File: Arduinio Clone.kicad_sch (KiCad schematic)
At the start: 12 parts, among them U1 DS1337_GM, U2 24LC1025, U3 ATmega328P-A, Y1 Crystal, Y2 Crystal

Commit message: Component associations and values
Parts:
- BT1: value Battery -> (none)
- C1, C2: value C -> (none)
- C3: value C_Polarized -> (none)
- D1: value LED -> (none)
- R1, R2: value R -> (none)
- U1: value DS1337_GM -> (none)
- U2: value 24LC1025 -> (none)
- U3: value ATmega328P-A -> (none); footprint Package_QFP:TQFP-32_7x7mm_P0.8mm -> (none)
- Y1, Y2: value Crystal -> (none)
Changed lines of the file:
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@@
     (in_bom yes) (on_board yes) (fields_autoplaced)
     (property "Reference" "D1" (id 0) (at 127.9525 68.58 0))
-    (property "Value" "LED" (id 1) (at 127.9525 71.12 0))
+    (property "Value" "" (id 1) (at 127.9525 71.12 0))
     (property "Footprint" "" (id 2) (at 129.54 74.93 0)
       (effects (font (size 1.27 1.27)) hide)
@@
       (effects (font (size 1.27 1.27)) (justify left))
     )
-    (property "Value" "24LC1025" (id 1) (at 51.5494 91.44 0)
+    (property "Value" "" (id 1) (at 51.5494 91.44 0)
       (effects (font (size 1.27 1.27)) (justify left))
     )
@@
     (in_bom yes) (on_board yes) (fields_autoplaced)
     (property "Reference" "Y1" (id 0) (at 29.21 60.96 0))
-    (property "Value" "Crystal" (id 1) (at 29.21 63.5 0))
+    (property "Value" "" (id 1) (at 29.21 63.5 0))
     (property "Footprint" "" (id 2) (at 29.21 68.58 0)
       (effects (font (size 1.27 1.27)) hide)
@@
       (effects (font (size 1.27 1.27)) (justify left))
     )
-    (property "Value" "C_Polarized" (id 1) (at 223.52 79.1209 0)
+    (property "Value" "" (id 1) (at 223.52 79.1209 0)
       (effects (font (size 1.27 1.27)) (justify left))
     )
@@
       (effects (font (size 1.27 1.27)) (justify left))
     )
-    (property "Value" "DS1337_GM" (id 1) (at 51.5494 63.5 0)
+    (property "Value" "" (id 1) (at 51.5494 63.5 0)
       (effects (font (size 1.27 1.27)) (justify left))
     )
@@
     (pin "8")
   )
+  (symbol (lib_id "power:GND") (at 218.44 114.3 0) (unit 1)
+    (in_bom yes) (on_board yes) (fields_autoplaced)
+    (property "Reference" "#PWR0101" (id 0) (at 218.44 120.65 0)
+      (effects (font (size 1.27 1.27)) hide)
+    )
+    (property "Value" "" (id 1) (at 218.44 119.38 0))
+    (property "Footprint" "" (id 2) (at 218.44 114.3 0)
+      (effects (font (size 1.27 1.27)) hide)
+    )
+    (property "Datasheet" "" (id 3) (at 218.44 114.3 0)
+      (effects (font (size 1.27 1.27)) hide)
+    )
+    (pin "1")
+  )
   (symbol (lib_id "MCU_Microchip_ATmega:ATmega328P-A") (at 163.83 86.36 0) (unit 1)
     (in_bom yes) (on_board yes) (fields_autoplaced)
@@
       (effects (font (size 1.27 1.27)) (justify left))
     )
-    (property "Value" "ATmega328P-A" (id 1) (at 165.8494 127 0)
-      (effects (font (size 1.27 1.27)) (justify left))
-    )
-    (property "Footprint" "Package_QFP:TQFP-32_7x7mm_P0.8mm" (id 2) (at 163.83 86.36 0)
+    (property "Value" "" (id 1) (at 165.8494 127 0)
+      (effects (font (size 1.27 1.27)) (justify left))
+    )
+    (property "Footprint" "" (id 2) (at 163.83 86.36 0)
       (effects (font (size 1.27 1.27) italic) hide)
     )
@@
       (effects (font (size 1.27 1.27)) (justify left))
     )
-    (property "Value" "C" (id 1) (at 95.25 57.1499 0)
+    (property "Value" "" (id 1) (at 95.25 57.1499 0)
       (effects (font (size 1.27 1.27)) (justify left))
     )
@@
       (effects (font (size 1.27 1.27)) (justify left))
     )
-    (property "Value" "R" (id 1) (at 115.57 86.3599 0)
+    (property "Value" "" (id 1) (at 115.57 86.3599 0)
       (effects (font (size 1.27 1.27)) (justify left))
     )
@@
       (effects (font (size 1.27 1.27)) (justify left))
     )
-    (property "Value" "Battery" (id 1) (at 223.52 59.3089 0)
+    (property "Value" "" (id 1) (at 223.52 59.3089 0)
       (effects (font (size 1.27 1.27)) (justify left))
     )
@@
     (in_bom yes) (on_board yes) (fields_autoplaced)
     (property "Reference" "Y2" (id 0) (at 102.87 60.96 0))
-    (property "Value" "Crystal" (id 1) (at 102.87 63.5 0))
+    (property "Value" "" (id 1) (at 102.87 63.5 0))
     (property "Footprint" "" (id 2) (at 102.87 68.58 0)
       (effects (font (size 1.27 1.27)) hide)
@@
       (effects (font (size 1.27 1.27)) (justify left))
     )
-    (property "Value" "R" (id 1) (at 135.89 93.9799 0)
+    (property "Value" "" (id 1) (at 135.89 93.9799 0)
       (effects (font (size 1.27 1.27)) (justify left))
     )
@@
       (effects (font (size 1.27 1.27)) (justify left))
     )
-    (property "Value" "C" (id 1) (at 95.25 67.3099 0)
+    (property "Value" "" (id 1) (at 95.25 67.3099 0)
       (effects (font (size 1.27 1.27)) (justify left))
     )
@@
   )
   (symbol_instances
+    (path "/7ea0c4cd-c3ff-478c-a95a-bb805f72808a"
+      (reference "#PWR0101") (unit 1) (value "GND") (footprint "")
+    )
     (path "/cb99d522-d98f-4f2e-af24-39a642a2262c"
-      (reference "BT1") (unit 1) (value "Battery") (footprint "")
+      (reference "BT1") (unit 1) (value "Battery 3V") (footprint "Connector_PinHeader_2.54mm:PinHeader_1x02_P2.54mm_Vertical")
     )
     (path "/a0a7411e-2ace-431e-9190-e1efd84cfa19"
-      (reference "C1") (unit 1) (value "C") (footprint "")
+      (reference "C1") (unit 1) (value "220pF") (footprint "Capacitor_SMD:C_0805_2012Metric")
     )
     (path "/f4cd744f-86c3-401e-9dc4-f3966535b983"
-      (reference "C2") (unit 1) (value "C") (footprint "")
+      (reference "C2") (unit 1) (value "220pF") (footprint "Capacitor_SMD:C_0805_2012Metric")
     )
     (path "/47ac9772-3d12-4e4c-be34-49c86c4d11b8"
-      (reference "C3") (unit 1) (value "C_Polarized") (footprint "")
+      (reference "C3") (unit 1) (value "10uF") (footprint "Capacitor_SMD:C_0805_2012Metric")
     )
     (path "/10f0ad0a-5347-4cd8-9e8b-b551768717e1"
-      (reference "D1") (unit 1) (value "LED") (footprint "")
+      (reference "D1") (unit 1) (value "LED") (footprint "LED_SMD:LED_0805_2012Metric")
     )
     (path "/99dcd93f-6742-4b81-a071-043df0a32b88/dd61ea61-ee00-483a-9cf3-44579a861992"
-      (reference "J1") (unit 1) (value "Conn_01x04") (footprint "")
+      (reference "J1") (unit 1) (value "Serial") (footprint "Connector_PinHeader_2.54mm:PinHeader_1x04_P2.54mm_Vertical")
     )
     (path "/99dcd93f-6742-4b81-a071-043df0a32b88/627a6bb9-dcd8-4955-91b8-8ac1c7ba0267"
-      (reference "J2") (unit 1) (value "Conn_01x09") (footprint "")
+      (reference "J2") (unit 1) (value "Digital Pins") (footprint "Connector_PinHeader_2.54mm:PinHeader_1x09_P2.54mm_Vertical")
     )
     (path "/99dcd93f-6742-4b81-a071-043df0a32b88/70a1e371-96bd-43fc-8ac7-1645345d3e46"
-      (reference "J3") (unit 1) (value "Conn_02x03_Odd_Even") (footprint "")
+      (reference "J3") (unit 1) (value "ICSP") (footprint "Connector_PinHeader_2.54mm:PinHeader_2x03_P2.54mm_Vertical")
     )
     (path "/99dcd93f-6742-4b81-a071-043df0a32b88/b8095f78-b7cb-4edb-8f3b-82dfbdf61388"
-      (reference "J4") (unit 1) (value "Conn_01x04") (footprint "")
+      (reference "J4") (unit 1) (value "I2C") (footprint "Connector_PinHeader_2.54mm:PinHeader_1x04_P2.54mm_Vertical")
     )
     (path "/a514a1f9-319e-4854-bd4a-fb2006c92301"
-      (reference "R1") (unit 1) (value "R") (footprint "")
+      (reference "R1") (unit 1) (value "330") (footprint "Resistor_SMD:R_0805_2012Metric_Pad1.20x1.40mm_HandSolder")
     )
     (path "/e1e0cd89-7085-4b67-b9fa-c00a933b2bea"
-      (reference "R2") (unit 1) (value "R") (footprint "")
+      (reference "R2") (unit 1) (value "10k") (footprint "Resistor_SMD:R_0805_2012Metric_Pad1.20x1.40mm_HandSolder")
     )
     (path "/5184beda-4204-4a1a-836c-6ca14ccda6ee"
-      (reference "U1") (unit 1) (value "DS1337_GM") (footprint "")
+      (reference "U1") (unit 1) (value "DS1337_GM") (footprint "Package_SO:SO-8_5.3x6.2mm_P1.27mm")
     )
     (path "/243ad795-d45f-41d7-b66a-04b2d1180b1c"
-      (reference "U2") (unit 1) (value "24LC1025") (footprint "")
+      (reference "U2") (unit 1) (value "24LC1025") (footprint "Package_SO:SOIC-8_3.9x4.9mm_P1.27mm")
     )
     (path "/7f29ecb0-6265-4d60-8278-7704387a2057"
@@
     )
     (path "/3fb113a1-a012-4b2e-a31d-61ea5b0c93b6"
-      (reference "Y1") (unit 1) (value "Crystal") (footprint "")
+      (reference "Y1") (unit 1) (value "Crystal 32MHz") (footprint "Crystal:Crystal_SMD_MicroCrystal_CC7V-T1A-2Pin_3.2x1.5mm")
     )
     (path "/d8dd4a5f-dc16-4ac5-8b31-704bbe349563"
-      (reference "Y2") (unit 1) (value "Crystal") (footprint "")
-    )
-  )
+      (reference "Y2") (unit 1) (value "Crystal 16MHz") (footprint "Crystal:Crystal_SMD_5032-2Pin_5.0x3.2mm_HandSoldering")
+    )
+  )

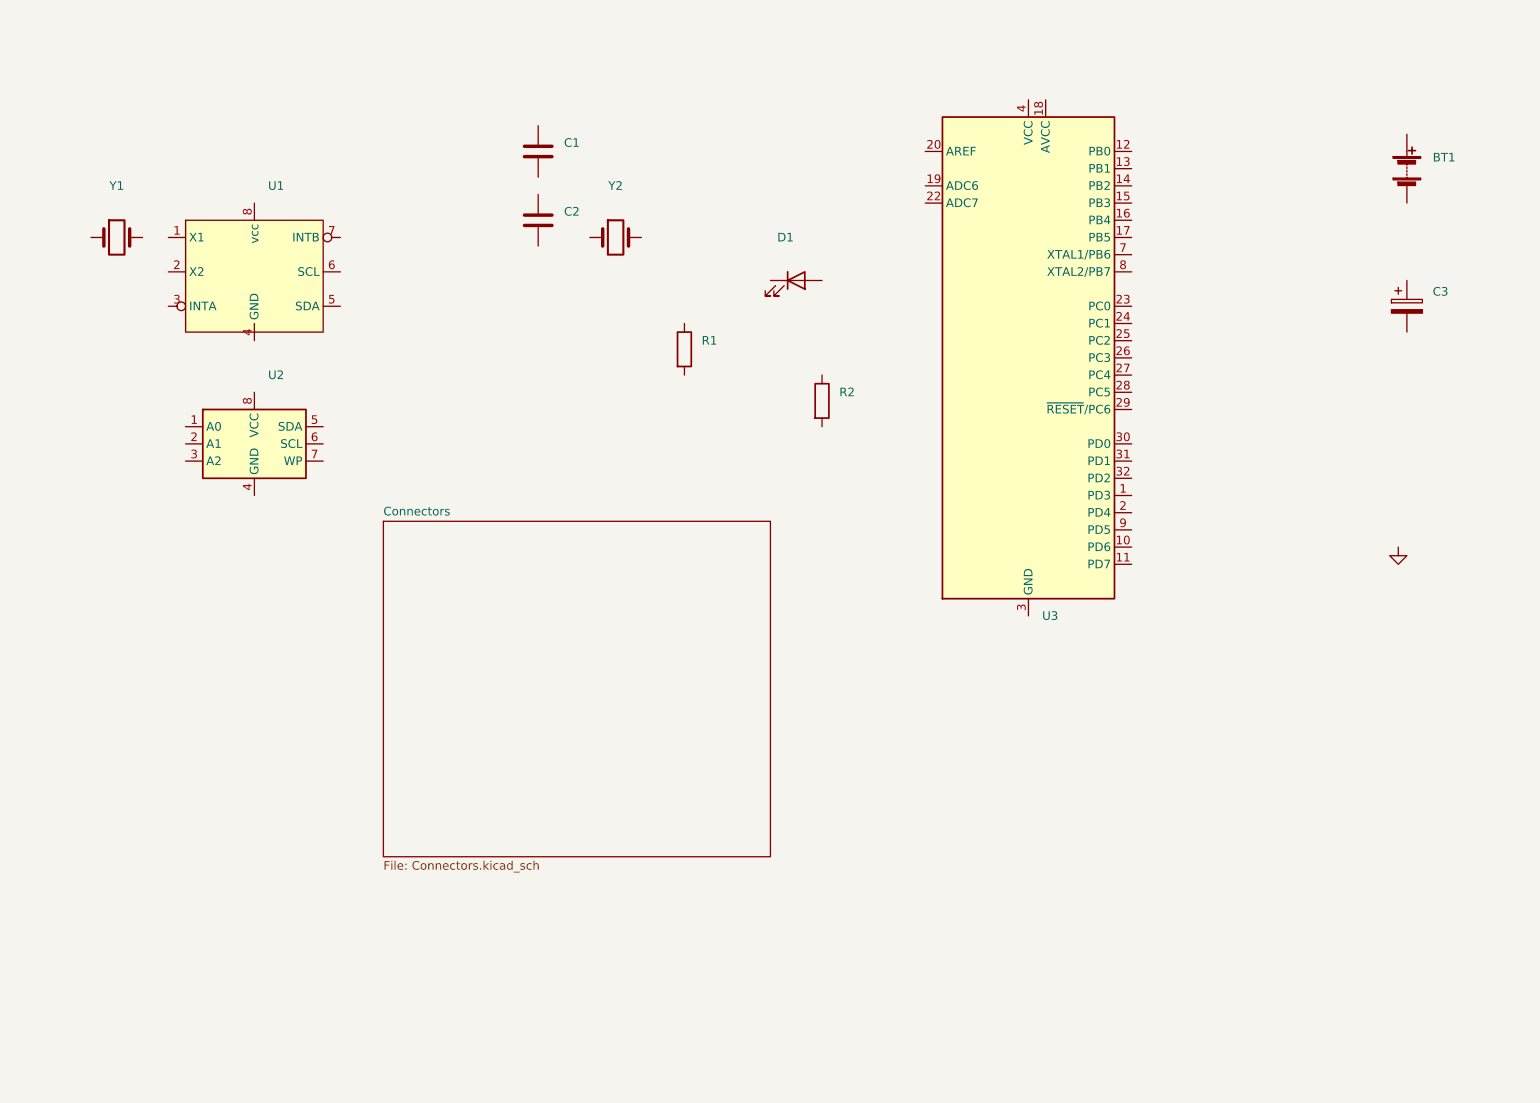
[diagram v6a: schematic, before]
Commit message: Connectors sheet wiring
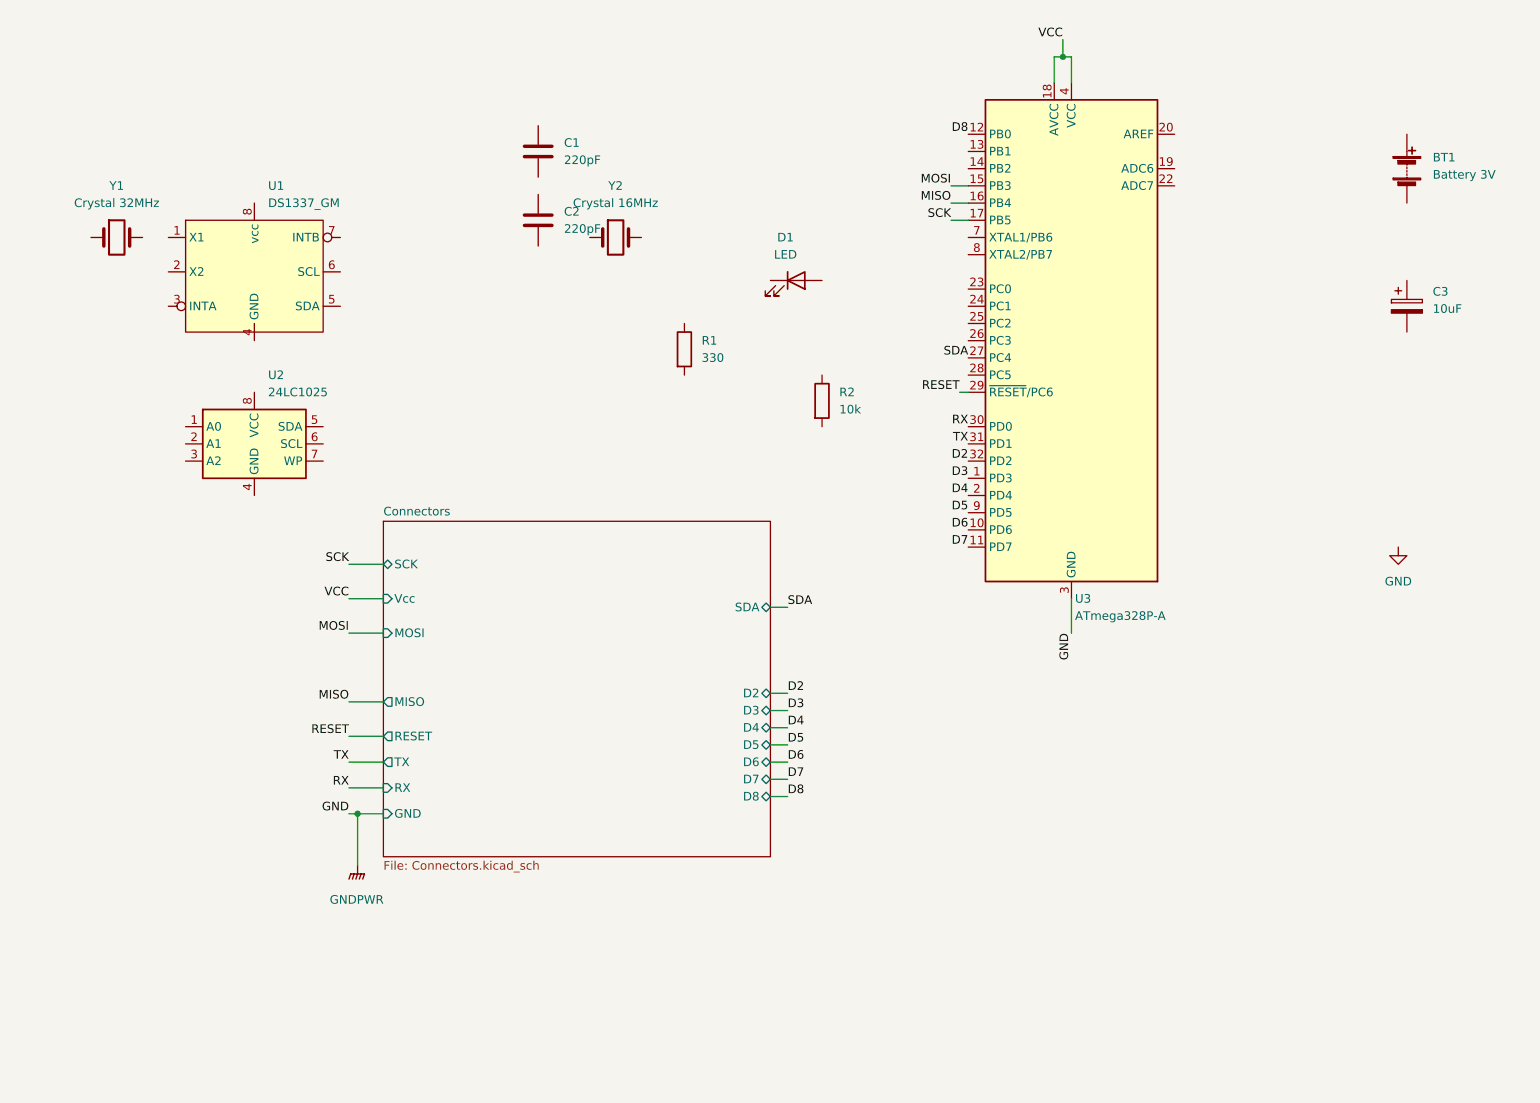
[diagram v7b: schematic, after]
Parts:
- BT1: value (none) -> Battery 3V; footprint (none) -> Connector_PinHeader_2.54mm:PinHeader_1x02_P2.54mm_Vertical
- C1, C2: value (none) -> 220pF; footprint (none) -> Capacitor_SMD:C_0805_2012Metric
- C3: value (none) -> 10uF; footprint (none) -> Capacitor_SMD:C_0805_2012Metric
- D1: value (none) -> LED; footprint (none) -> LED_SMD:LED_0805_2012Metric
- R1: value (none) -> 330; footprint (none) -> Resistor_SMD:R_0805_2012Metric_Pad1.20x1.40mm_HandSolder
- R2: value (none) -> 10k; footprint (none) -> Resistor_SMD:R_0805_2012Metric_Pad1.20x1.40mm_HandSolder
- U1: value (none) -> DS1337_GM; footprint (none) -> Package_SO:SO-8_5.3x6.2mm_P1.27mm
- U2: value (none) -> 24LC1025; footprint (none) -> Package_SO:SOIC-8_3.9x4.9mm_P1.27mm
- U3: value (none) -> ATmega328P-A; footprint (none) -> Package_QFP:TQFP-32_7x7mm_P0.8mm
- Y1: value (none) -> Crystal 32MHz; footprint (none) -> Crystal:Crystal_SMD_MicroCrystal_CC7V-T1A-2Pin_3.2x1.5mm
- Y2: value (none) -> Crystal 16MHz; footprint (none) -> Crystal:Crystal_SMD_5032-2Pin_5.0x3.2mm_HandSoldering
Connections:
- net GND: now also U3.21 (GND), U3.3 (GND), U3.5 (GND)
- net D3: now reaches U3.1 (PD3)
- net D6: now reaches U3.10 (PD6)
- net D7: now reaches U3.11 (PD7)
- net D8: now reaches U3.12 (PB0)
- net MOSI: now reaches U3.15 (PB3)
- net MISO: now reaches U3.16 (PB4)
- net SCK: now reaches U3.17 (PB5)
- net VCC: now reaches U3.18 (AVCC)
- net VCC: now also U3.4 (VCC), U3.6 (VCC)
- net D4: now reaches U3.2 (PD4)
- net SDA: now reaches U3.27 (PC4)
- net RESET: now reaches U3.29 (~{RESET}/PC6)
- net RX: now reaches U3.30 (PD0)
- net TX: now reaches U3.31 (PD1)
- net D2: now reaches U3.32 (PD2)
- net D5: now reaches U3.9 (PD5)
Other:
- sheet Connectors ports: added D2, D3, D4, D5, D6, D7, D8, GND, MISO, MOSI, RESET, RX, SCK, SDA, TX, Vcc; removed none
- moved on the sheet: U3

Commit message: Root sheet wiring
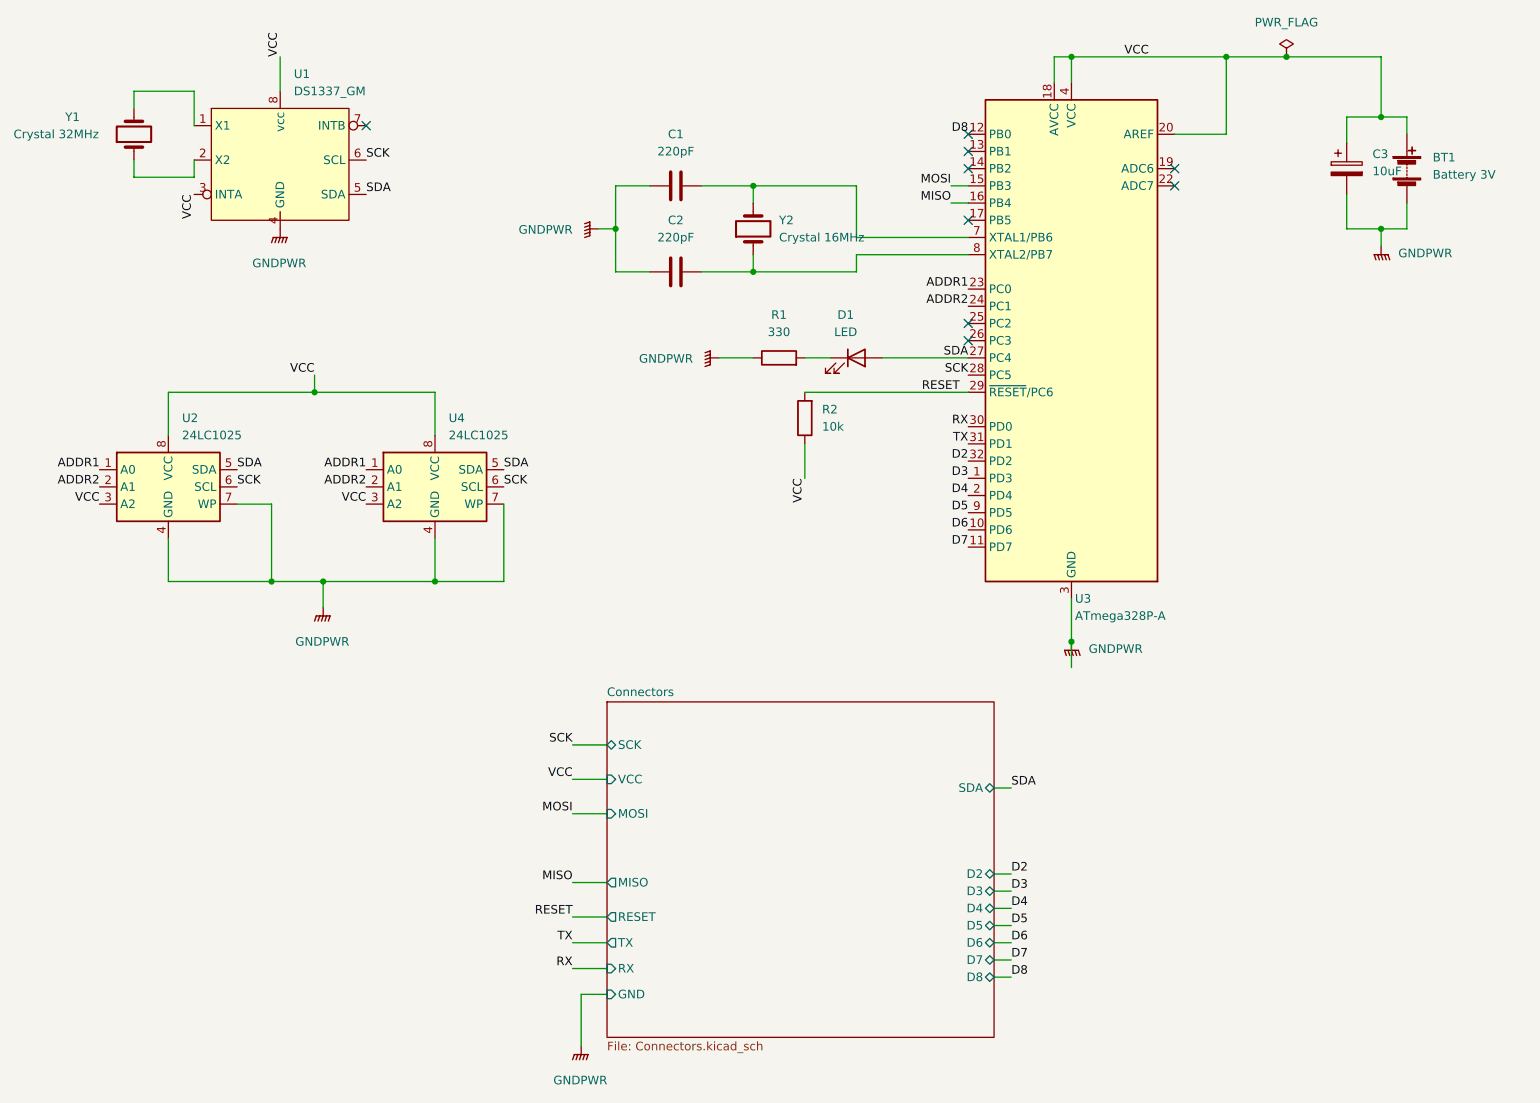
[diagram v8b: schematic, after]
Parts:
- added U4: 24LC1025, Package_SO:SOIC-8_3.9x4.9mm_P1.27mm, symbol Memory_EEPROM:24LC1025
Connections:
- net GND is gone; now on net GNDPWR: U3.21 (GND), U3.3 (GND), U3.5 (GND)
- net RESET: now also R2.2
- net SCK: now also U1.6 (SCL), U2.6 (SCL), U3.28 (PC5), U4.6 (SCL); no longer U3.17 (PB5)
- net SDA: now also D1.2 (A), U1.5 (SDA), U2.5 (SDA), U4.5 (SDA)
- net VCC: now also BT1.1 (+), C3.1, R2.1, U1.3 (INTA), U1.8 (vcc), U2.3 (A2), U2.8 (VCC), U3.20 (AREF), U4.3 (A2), U4.8 (VCC)
- net at D1.1 (K): now also R1.2
- net ADDR1: now reaches U2.1 (A0)
- net ADDR1: now also U3.23 (PC0), U4.1 (A0)
- net ADDR2: now reaches U2.2 (A1)
- net ADDR2: now also U3.24 (PC1), U4.2 (A1)
- net GNDPWR: now reaches U2.4 (GND)
- net GNDPWR: now also BT1.2 (-), C1.1, C2.1, C3.2, R1.1, U1.4 (GND), U2.7 (WP), U4.4 (GND), U4.7 (WP)
- net at Y1.1: now also U1.2 (X2)
- net at Y1.2: now also U1.1 (X1)
- net at U3.7 (XTAL1/PB6): now also C1.2, Y2.2
- net at U3.8 (XTAL2/PB7): now also C2.2, Y2.1
- no-connect marks 0 -> 9
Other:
- sheet Connectors ports: added VCC; removed Vcc
- moved on the sheet: C1, C2, C3, D1, R1, R2, U1, U2, Y1, Y2
